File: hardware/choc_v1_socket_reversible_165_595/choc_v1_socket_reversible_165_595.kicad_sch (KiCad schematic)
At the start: 76 parts, among them SW00 SW_Push, SW01 SW_Push, SW02 SW_Push, SW03 SW_Push, SW04 SW_Push, SW05 SW_Push, SW10 SW_Push, SW11 SW_Push, SW12 SW_Push, SW13 SW_Push, SW14 SW_Push, SW15 SW_Push, SW20 SW_Push, SW21 SW_Push, SW22 SW_Push, SW23 SW_Push, SW24 SW_Push, SW25 SW_Push, SW30 SW_Push, SW31 SW_Push, SW32 SW_Push, SW33 SW_Push, SW34 SW_Push, SW35 SW_Push, SW36 SW_Push, SW37 SW_Push, U1 CH582

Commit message: Cleaned up footprint library, added new design, updated python script
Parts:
- removed D0001, D0203, D0405, D1011, D1213, D1415, D2021, D2223, D2425, D3031, D3233, D3435, D3637: BAV70, keyswitches:BAV70_SOT-23_Reversible, symbol Diode:BAV70
- removed SW37: SW_Push, keyswitches:Kailh_socket_PG1350_reversible, symbol Switch:SW_Push
- added D0, D1, D2, D3, D4, D5, D6: BAW56DW, reversible_kbd:BAW70DW_reversible, symbol Diode:BAW56DW
- added SW26: SW_Push, keyswitches:Kailh_socket_PG1350_reversible, symbol Switch:SW_Push
- LED00, LED01, LED02, LED03, LED04, LED05, LED10, LED11, LED12, LED13, LED14, LED15, LED20, LED21, LED22, LED23, LED24, LED25, LED30, LED31, LED32, LED33, LED34, LED35: footprint keyswitches:LED_SK6812MINI_E_REVERSIBLE_1 -> reversible_kbd:LED_SK6812MINI_E_REVERSIBLE
- LED26: renamed from LED36; footprint keyswitches:LED_SK6812MINI_E_REVERSIBLE_1 -> reversible_kbd:LED_SK6812MINI_E_REVERSIBLE
- LED36: renamed from LED37; footprint keyswitches:LED_SK6812MINI_E_REVERSIBLE_1 -> reversible_kbd:LED_SK6812MINI_E_REVERSIBLE
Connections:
- net COL0: now also D0.3 (A), D0.3 (A), D0.6 (A), D0.6 (A); no longer SW00.1, SW10.1, SW20.1, SW30.1
- net COL1: now also D1.3 (A), D1.3 (A), D1.6 (A), D1.6 (A); no longer SW01.1, SW11.1, SW21.1, SW31.1
- net COL2: now also D2.3 (A), D2.3 (A), D2.6 (A), D2.6 (A); no longer SW02.1, SW12.1, SW22.1, SW32.1
- net COL3: now also D3.3 (A), D3.3 (A), D3.6 (A), D3.6 (A); no longer SW03.1, SW13.1, SW23.1, SW33.1
- net COL4: now also D4.3 (A), D4.3 (A), D4.6 (A), D4.6 (A); no longer SW04.1, SW14.1, SW24.1, SW34.1
- net COL5: now also D5.3 (A), D5.3 (A), D5.6 (A), D5.6 (A); no longer SW05.1, SW15.1, SW25.1, SW35.1
- net COL6: now also D6.3 (A), D6.3 (A); no longer SW36.1
- net ROW0: now also SW00.2, SW01.2, SW02.2, SW03.2, SW04.2, SW05.2
- net ROW1: now also SW10.2, SW11.2, SW12.2, SW13.2, SW14.2, SW15.2
- net ROW2: now also SW20.2, SW21.2, SW22.2, SW23.2, SW24.2, SW25.2, SW26.2
- net ROW3: now also SW30.2, SW31.2, SW32.2, SW33.2, SW34.2, SW35.2, SW36.2
- new net: D1.2 (K), SW11.1
- new net: D2.4 (K), SW22.1
- new net: D1.4 (K), SW21.1
- new net: D4.2 (K), SW14.1
- new net: D1.5 (K), SW31.1
- new net: D3.5 (K), SW33.1
- new net: D5.4 (K), SW25.1
- new net: D0.4 (K), SW20.1
- new net: D5.5 (K), SW35.1
- new net: D5.1 (K), SW05.1
- new net: D0.2 (K), SW10.1
- new net: D0.5 (K), SW30.1
- new net: D3.2 (K), SW13.1
- new net: D2.5 (K), SW32.1
- new net: D2.2 (K), SW12.1
- new net: D3.4 (K), SW23.1
- new net: D6.4 (K), SW26.1
- new net: D1.1 (K), SW01.1
- new net: D4.1 (K), SW04.1
- new net: D2.1 (K), SW02.1
- new net: D0.1 (K), SW00.1
- new net: D6.5 (K), SW36.1
- new net: D3.1 (K), SW03.1
- new net: D5.2 (K), SW15.1
- new net: D4.5 (K), SW34.1
- new net: D4.4 (K), SW24.1
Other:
- moved on the sheet: J_LEFT1, J_RIGHT1, R1, RN_LEFT1, RN_RIGHT1, SR_LEFT1, SR_RIGHT1, SW00, SW10, SW20, SW30, U1

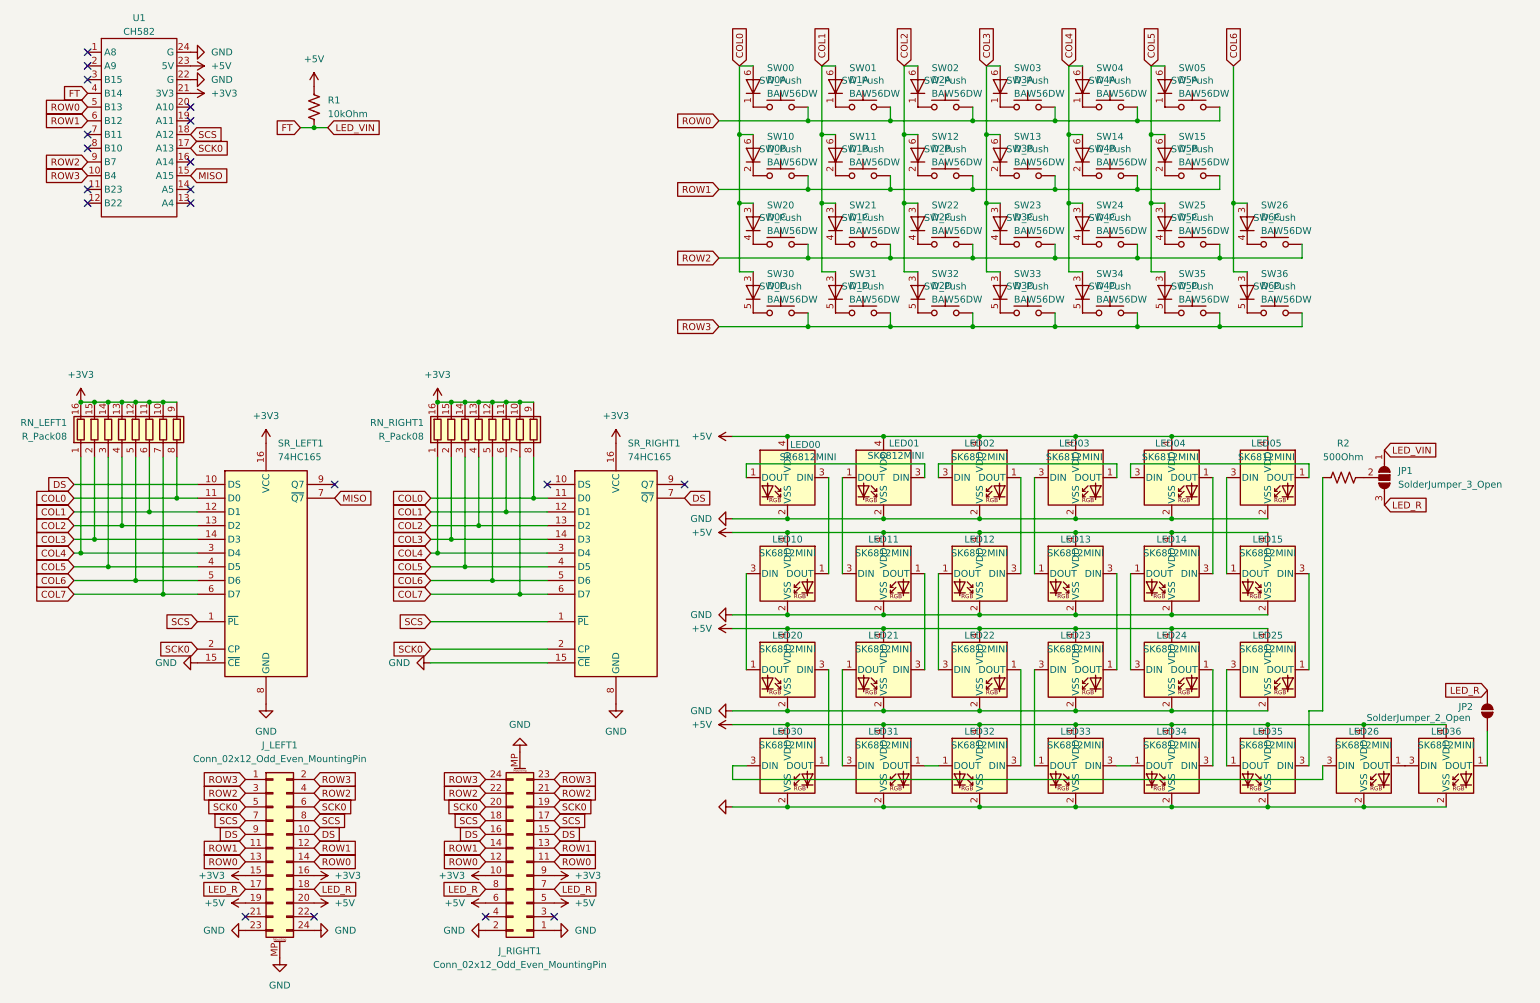
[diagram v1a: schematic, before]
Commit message: Improved switch and led routing, cleaned up script
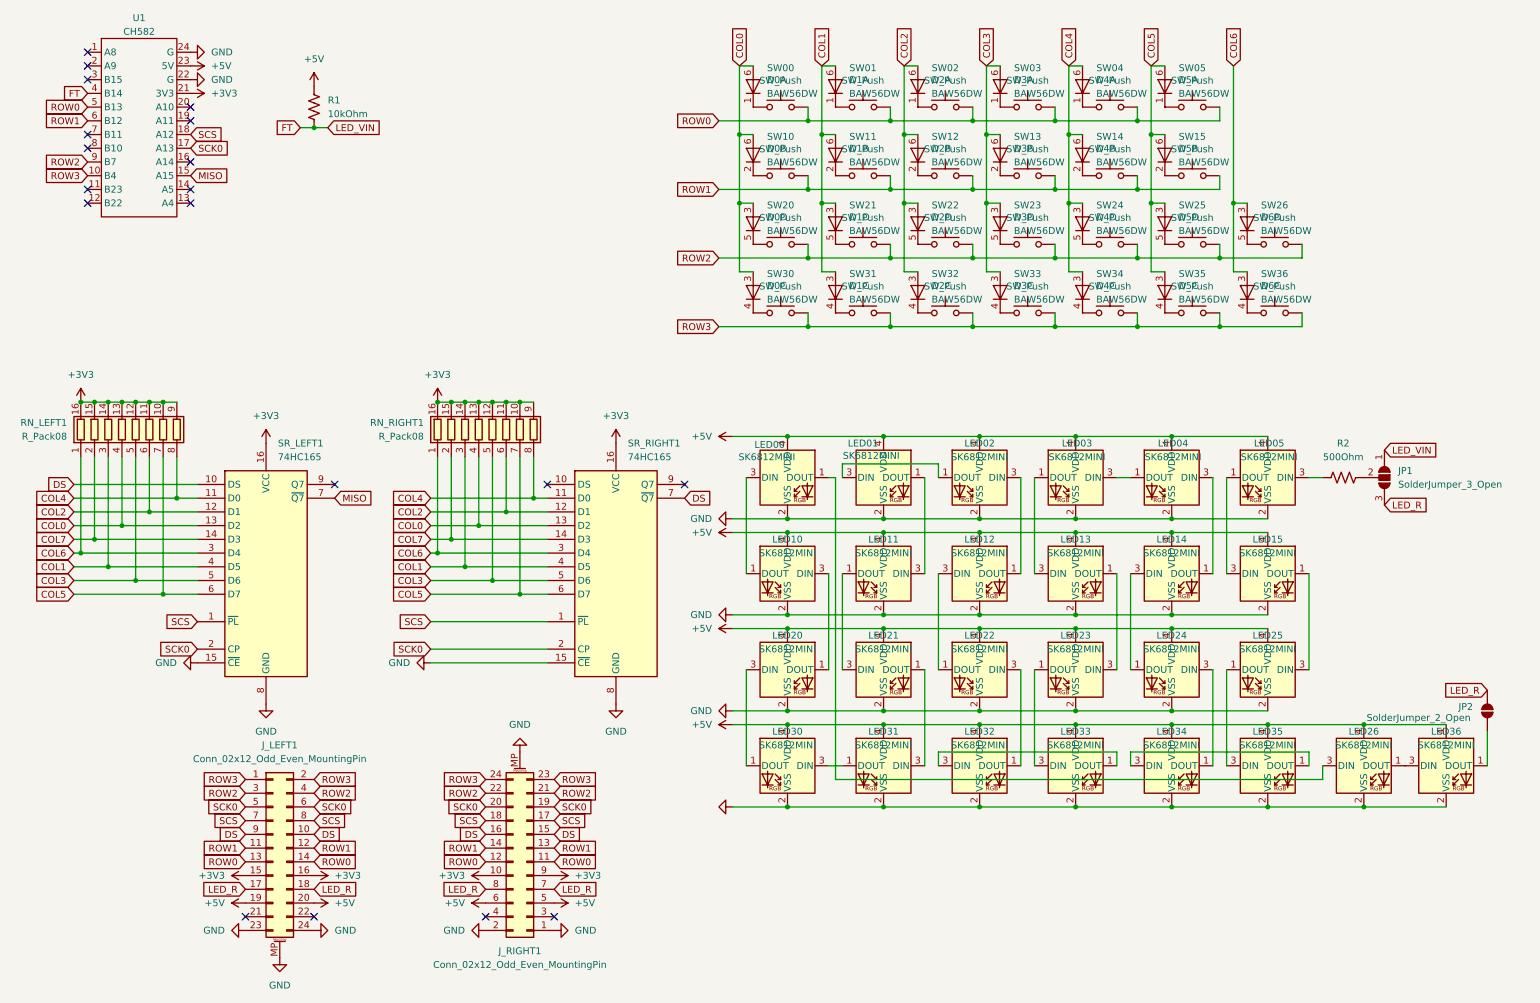
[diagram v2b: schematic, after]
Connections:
- net COL0: now also RN_LEFT1.4 (R4.1), RN_RIGHT1.4 (R4.1), SR_LEFT1.13 (D2), SR_RIGHT1.13 (D2); no longer RN_LEFT1.8 (R8.1), RN_RIGHT1.8 (R8.1), SR_LEFT1.11 (D0), SR_RIGHT1.11 (D0)
- net COL1: now also RN_LEFT1.3 (R3.1), RN_RIGHT1.3 (R3.1), SR_LEFT1.4 (D5), SR_RIGHT1.4 (D5); no longer RN_LEFT1.6 (R6.1), RN_RIGHT1.6 (R6.1), SR_LEFT1.12 (D1), SR_RIGHT1.12 (D1)
- net COL2: now also RN_LEFT1.6 (R6.1), RN_RIGHT1.6 (R6.1), SR_LEFT1.12 (D1), SR_RIGHT1.12 (D1); no longer RN_LEFT1.4 (R4.1), RN_RIGHT1.4 (R4.1), SR_LEFT1.13 (D2), SR_RIGHT1.13 (D2)
- net COL3: now also RN_LEFT1.5 (R5.1), RN_RIGHT1.5 (R5.1), SR_LEFT1.5 (D6), SR_RIGHT1.5 (D6); no longer RN_LEFT1.2 (R2.1), RN_RIGHT1.2 (R2.1), SR_LEFT1.14 (D3), SR_RIGHT1.14 (D3)
- net COL4: now also RN_LEFT1.8 (R8.1), RN_RIGHT1.8 (R8.1), SR_LEFT1.11 (D0), SR_RIGHT1.11 (D0); no longer RN_LEFT1.1 (R1.1), RN_RIGHT1.1 (R1.1), SR_LEFT1.3 (D4), SR_RIGHT1.3 (D4)
- net COL5: now also RN_LEFT1.7 (R7.1), RN_RIGHT1.7 (R7.1), SR_LEFT1.6 (D7), SR_RIGHT1.6 (D7); no longer RN_LEFT1.3 (R3.1), RN_RIGHT1.3 (R3.1), SR_LEFT1.4 (D5), SR_RIGHT1.4 (D5)
- net COL6: now also RN_LEFT1.1 (R1.1), RN_RIGHT1.1 (R1.1), SR_LEFT1.3 (D4), SR_RIGHT1.3 (D4); no longer RN_LEFT1.5 (R5.1), RN_RIGHT1.5 (R5.1), SR_LEFT1.5 (D6), SR_RIGHT1.5 (D6)
- net COL7: now also RN_LEFT1.2 (R2.1), RN_RIGHT1.2 (R2.1), SR_LEFT1.14 (D3), SR_RIGHT1.14 (D3); no longer RN_LEFT1.7 (R7.1), RN_RIGHT1.7 (R7.1), SR_LEFT1.6 (D7), SR_RIGHT1.6 (D7)
- net at LED34.1 (DOUT): now also LED24.3 (DIN); no longer LED33.3 (DIN)
- net at LED34.3 (DIN): now also LED35.1 (DOUT); no longer LED24.1 (DOUT)
- net at LED22.1 (DOUT): now also LED12.3 (DIN); no longer LED32.3 (DIN)
- net at LED22.3 (DIN): now also LED32.1 (DOUT); no longer LED12.1 (DOUT)
- net at D2.4 (K): now also SW32.1; no longer SW22.1
- net at D1.4 (K): now also SW31.1; no longer SW21.1
- net at D1.5 (K): now also SW21.1; no longer SW31.1
- net at SW33.1: now also D3.4 (K); no longer D3.5 (K)
- net at D5.4 (K): now also SW35.1; no longer SW25.1
- net at SW20.1: now also D0.5 (K); no longer D0.4 (K)
- net at D5.5 (K): now also SW25.1; no longer SW35.1
- net at LED02.1 (DOUT): now also LED01.3 (DIN); no longer LED12.3 (DIN)
- net at LED02.3 (DIN): now also LED12.1 (DOUT); no longer LED03.1 (DOUT)
- net at SW30.1: now also D0.4 (K); no longer D0.5 (K)
- net at LED03.3 (DIN): now also LED04.1 (DOUT); no longer LED13.1 (DOUT)
- net at D2.5 (K): now also SW22.1; no longer SW32.1
- net at LED26.3 (DIN): now also LED00.1 (DOUT); no longer LED30.3 (DIN)
- net at LED14.3 (DIN): now also LED24.1 (DOUT); no longer LED04.1 (DOUT)
- net at LED04.3 (DIN): now also LED14.1 (DOUT); no longer LED05.1 (DOUT)
- net at SW23.1: now also D3.5 (K); no longer D3.4 (K)
- net at SW26.1: now also D6.5 (K); no longer D6.4 (K)
- net at LED25.1 (DOUT): now also LED35.3 (DIN); no longer LED15.3 (DIN)
- net at LED25.3 (DIN): now also LED15.1 (DOUT); no longer LED35.1 (DOUT)
- net at SW36.1: now also D6.4 (K); no longer D6.5 (K)
- net at LED13.3 (DIN): now also LED03.1 (DOUT); no longer LED23.1 (DOUT)
- net at LED23.3 (DIN): now also LED13.1 (DOUT); no longer LED33.1 (DOUT)
- net at LED31.1 (DOUT): now also LED30.3 (DIN); no longer LED32.1 (DOUT)
- net at R2.1: now also LED05.3 (DIN); no longer LED35.3 (DIN)
- net at SW34.1: now also D4.4 (K); no longer D4.5 (K)
- net at SW24.1: now also D4.5 (K); no longer D4.4 (K)
- new net: LED23.1 (DOUT), LED33.3 (DIN)
- new net: LED32.3 (DIN), LED33.1 (DOUT)
- new net: LED05.1 (DOUT), LED15.3 (DIN)
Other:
- moved on the sheet: D0C, D0D, D1C, D1D, D2C, D2D, D3C, D3D, D4C, D4D, D5C, D5D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

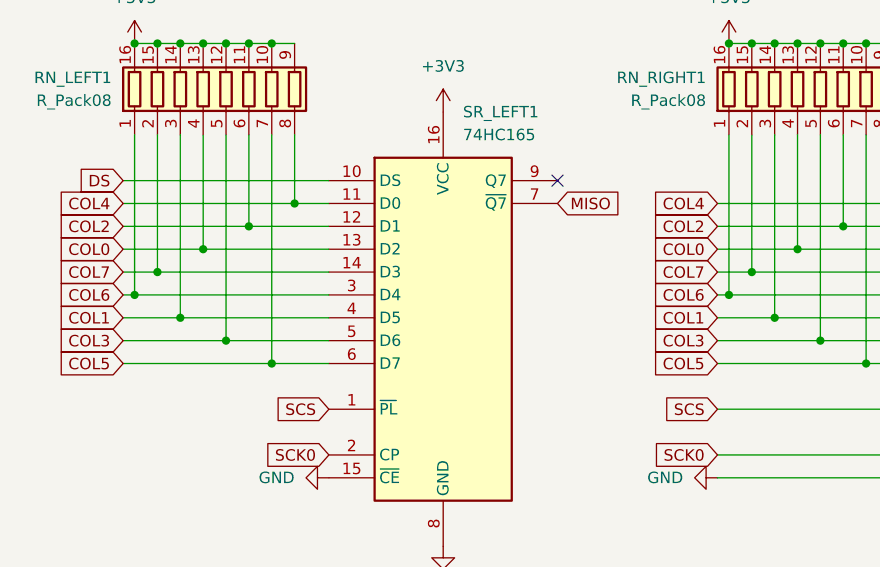
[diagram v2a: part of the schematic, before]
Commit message: Improved shift register - column routing
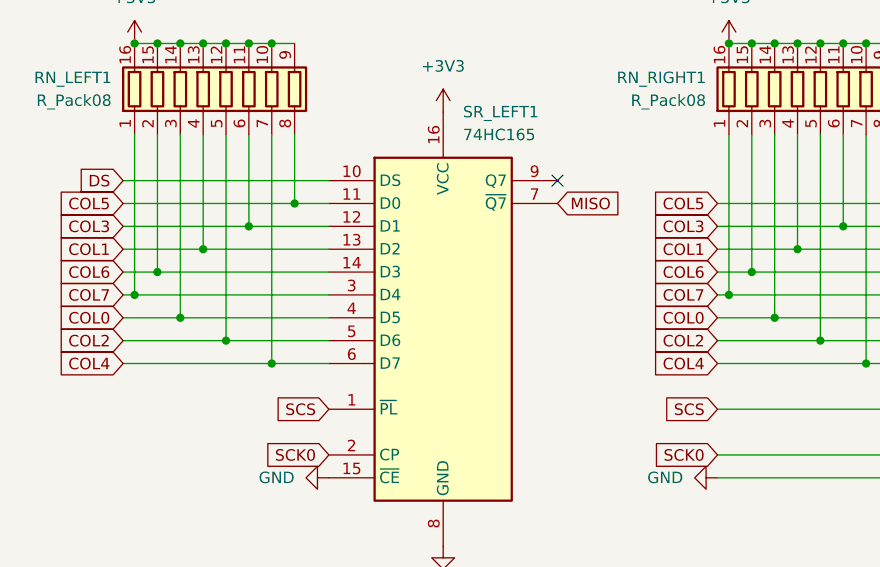
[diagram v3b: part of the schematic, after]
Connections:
- net COL0: now also RN_LEFT1.3 (R3.1), RN_RIGHT1.3 (R3.1), SR_LEFT1.4 (D5), SR_RIGHT1.4 (D5); no longer RN_LEFT1.4 (R4.1), RN_RIGHT1.4 (R4.1), SR_LEFT1.13 (D2), SR_RIGHT1.13 (D2)
- net COL1: now also RN_LEFT1.4 (R4.1), RN_RIGHT1.4 (R4.1), SR_LEFT1.13 (D2), SR_RIGHT1.13 (D2); no longer RN_LEFT1.3 (R3.1), RN_RIGHT1.3 (R3.1), SR_LEFT1.4 (D5), SR_RIGHT1.4 (D5)
- net COL2: now also RN_LEFT1.5 (R5.1), RN_RIGHT1.5 (R5.1), SR_LEFT1.5 (D6), SR_RIGHT1.5 (D6); no longer RN_LEFT1.6 (R6.1), RN_RIGHT1.6 (R6.1), SR_LEFT1.12 (D1), SR_RIGHT1.12 (D1)
- net COL3: now also RN_LEFT1.6 (R6.1), RN_RIGHT1.6 (R6.1), SR_LEFT1.12 (D1), SR_RIGHT1.12 (D1); no longer RN_LEFT1.5 (R5.1), RN_RIGHT1.5 (R5.1), SR_LEFT1.5 (D6), SR_RIGHT1.5 (D6)
- net COL4: now also RN_LEFT1.7 (R7.1), RN_RIGHT1.7 (R7.1), SR_LEFT1.6 (D7), SR_RIGHT1.6 (D7); no longer RN_LEFT1.8 (R8.1), RN_RIGHT1.8 (R8.1), SR_LEFT1.11 (D0), SR_RIGHT1.11 (D0)
- net COL5: now also RN_LEFT1.8 (R8.1), RN_RIGHT1.8 (R8.1), SR_LEFT1.11 (D0), SR_RIGHT1.11 (D0); no longer RN_LEFT1.7 (R7.1), RN_RIGHT1.7 (R7.1), SR_LEFT1.6 (D7), SR_RIGHT1.6 (D7)
- net COL6: now also RN_LEFT1.2 (R2.1), RN_RIGHT1.2 (R2.1), SR_LEFT1.14 (D3), SR_RIGHT1.14 (D3); no longer RN_LEFT1.1 (R1.1), RN_RIGHT1.1 (R1.1), SR_LEFT1.3 (D4), SR_RIGHT1.3 (D4)
- net COL7: now also RN_LEFT1.1 (R1.1), RN_RIGHT1.1 (R1.1), SR_LEFT1.3 (D4), SR_RIGHT1.3 (D4); no longer RN_LEFT1.2 (R2.1), RN_RIGHT1.2 (R2.1), SR_LEFT1.14 (D3), SR_RIGHT1.14 (D3)

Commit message: Finished layout
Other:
- moved on the sheet: R1, U1
